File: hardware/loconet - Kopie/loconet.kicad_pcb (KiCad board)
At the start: 2 copper layers, 91.4 x 73.3 mm, 46 parts, among them J1 RJ12, J10 PWR, J11 PullUpEnable, J2 RJ12, J3 DCC, J4 Arduino Sockelleiste Pin01-15, J5 Arduino Sockelleiste Pin16-30, J6 PCA9685, J7 SCL/SDA, J8 I²C Connector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

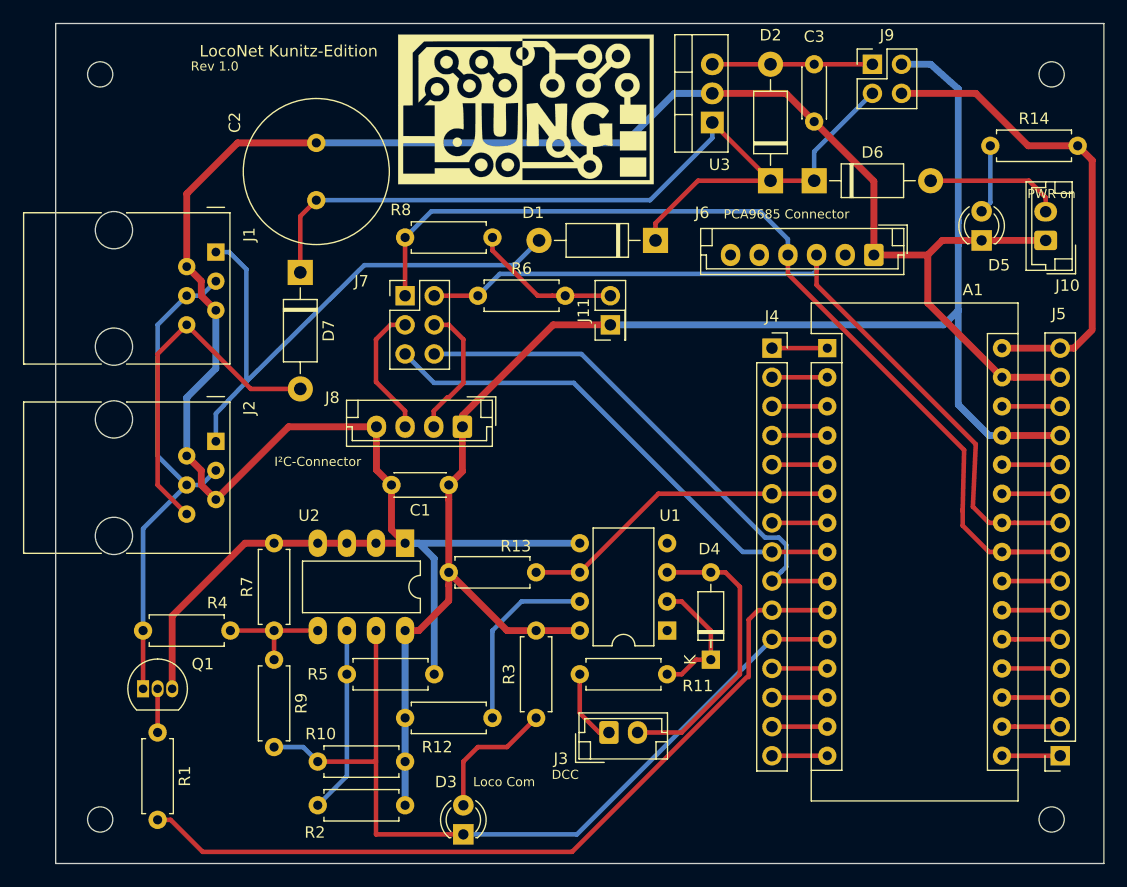
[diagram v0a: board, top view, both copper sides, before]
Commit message: Add variant hardware with loconet TX indicator LED
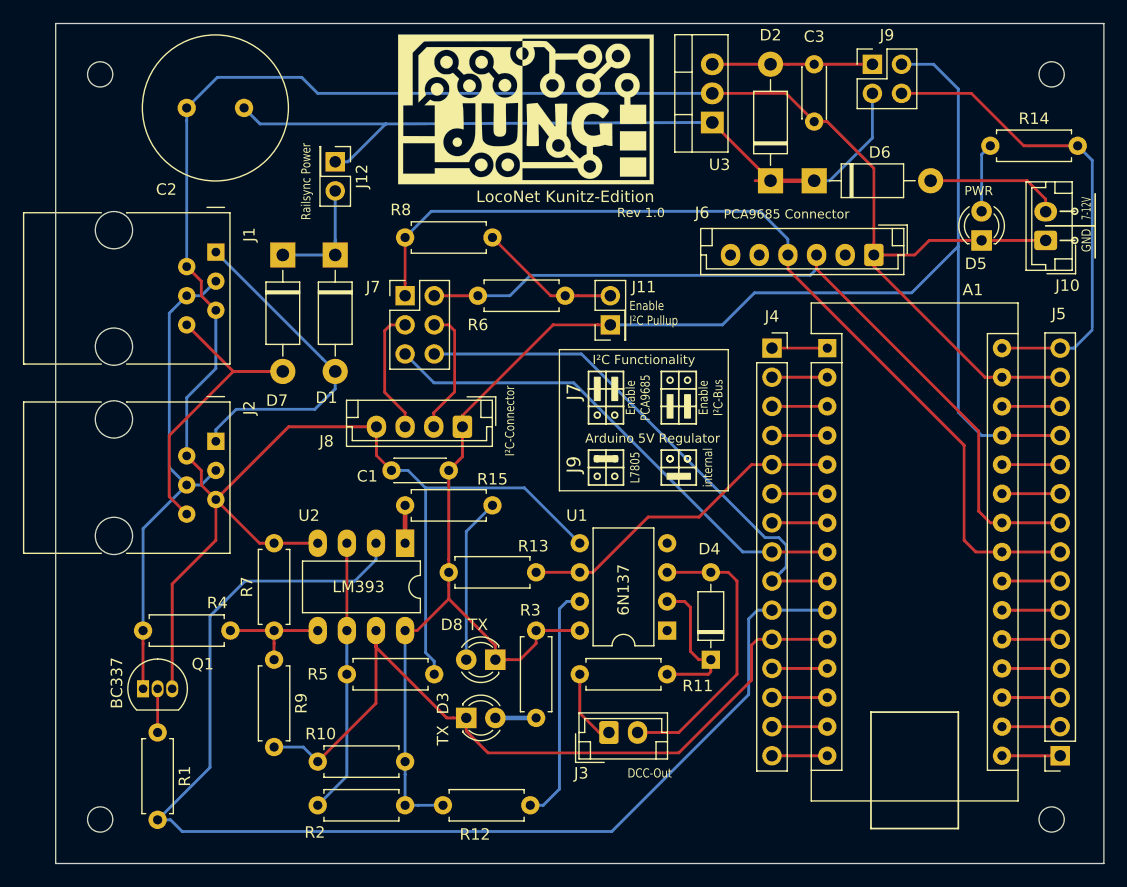
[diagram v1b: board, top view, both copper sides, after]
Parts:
- added D8: LocoTX, LED_THT:LED_D3.0mm, F.Cu at (236.5, 99.1)
- added J12: Railsync, Connector_PinHeader_2.54mm:PinHeader_2x01_P2.54mm_Vertical, F.Cu at (222.5, 55.6)
- added R15: 470k, Resistor_THT:R_Axial_DIN0207_L6.3mm_D2.5mm_P7.62mm_Horizontal, F.Cu at (236.2, 85.6)
- D3: value LocoCom -> LocoRX
- moved D1 28.0 mm to (222.5, 63.8), turned to 270 degrees
- moved C2 11.7 mm to (209.6, 50.9), turned to 0 degrees
- moved D3 10.2 mm to (233.9, 104.1), turned to 0 degrees
- moved R12 8.30 mm to (231.9, 111.8)
- moved D7 2.16 mm to (217.9, 63.8)
- moved C1 1.27 mm to (232.4, 82.5)
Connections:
- D1 pad 1: Vdrive -> Net-(D1-Pad1)
- D7 pad 1: Vdrive -> Net-(D1-Pad1)
- R2 pad 2: /Komperatorspannung -> U_Komperator
- R5 pad 1: /Komperatorspannung -> U_Komperator
- U2 pad 1: 29 -> Net-(R15-Pad2)
- U2 pad 2: 29 -> 10
- U2 pad 3: 29 -> U_Komperator
- U2 pad 6: /Komperatorspannung -> U_Komperator
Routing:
- net 10: track 71.1 -> 108.3 mm
- net U_Komperator: track 0.00 -> 23.9 mm
- net Net-(D1-Pad2): track 50.0 -> 29.2 mm
- net /Komperatorspannung: track 16.3 -> 0.00 mm
- net Net-(D8-Pad2): track 0.00 -> 14.4 mm
- net Net-(D1-Pad1): track 0.00 -> 11.5 mm
- net Vdrive: track 78.8 -> 70.1 mm
- net 29: track 222.5 -> 231.2 mm
- net Net-(D3-Pad2): track 11.7 -> 3.56 mm
- net 27: track 141.4 -> 149.3 mm
- net Net-(R12-Pad2): track 16.3 -> 20.9 mm
- net 11: track 73.6 -> 69.1 mm
- net Net-(R15-Pad2): track 0.00 -> 3.30 mm
- net Net-(D7-Pad2): track 30.8 -> 29.3 mm
- net Net-(D4-Pad1): track 11.7 -> 13.1 mm
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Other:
- board text added: "7-12V"
- board text added: "Arduino 5V Regulator"
- board text added: "DCC-Out"
- board text added: "Enable I²C Pullup"
- board text added: "Enable I²C-Bus"
- board text added: "Enable PCA9685"
- board text added: "GND"
- board text added: "I²C Functionality"
- board text added: "J7"
- board text added: "J9"
- board text added: "L7805"
- board text added: "PWR"
- board text added: "Railsync Power"
- board text added: "TX"
- board text added: "internal"
- board text removed: "DCC"
- board text removed: "Loco Com"
- board text removed: "PWR on"

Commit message: Einige Verbesserungen am PCB Layout
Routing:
- net Vdrive: track 70.1 -> 68.7 mm
- net 9: track 46.1 -> 46.9 mm
- net 11: track 69.1 -> 68.4 mm
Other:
- board text added: "1"
- board text added: "2"
- board text added: "3"
- board text added: "3V3"
- board text added: "4"
- board text added: "5"
- board text added: "5V"
- board text added: "6"
- board text added: "A0"
- board text added: "A1"
- board text added: "A2"
- board text added: "A3"
- board text added: "A4"
- board text added: "A5"
- board text added: "A6"
- board text added: "A7"
- board text added: "D10"
- board text added: "D11"
- board text added: "D12"
- board text added: "D13"
- board text added: "D2"
- board text added: "D3"
- board text added: "D4"
- board text added: "D5"
- board text added: "D6"
- board text added: "D7"
- board text added: "D8"
- board text added: "D9"
- board text added: "RST"
- board text added: "RX1"
- board text added: "TX1"
- board text added: "Vin"
- board text added: "Vref"

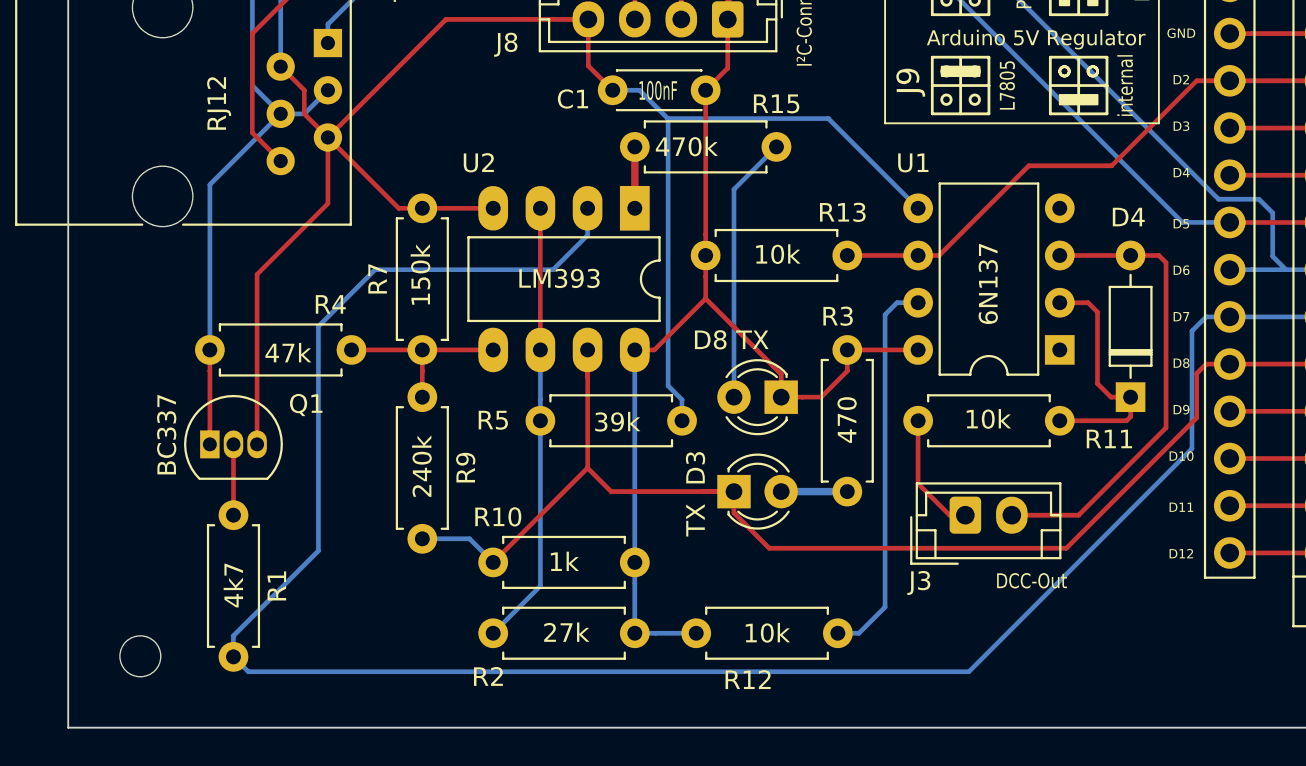
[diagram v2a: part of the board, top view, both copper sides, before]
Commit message: Added some capacitors
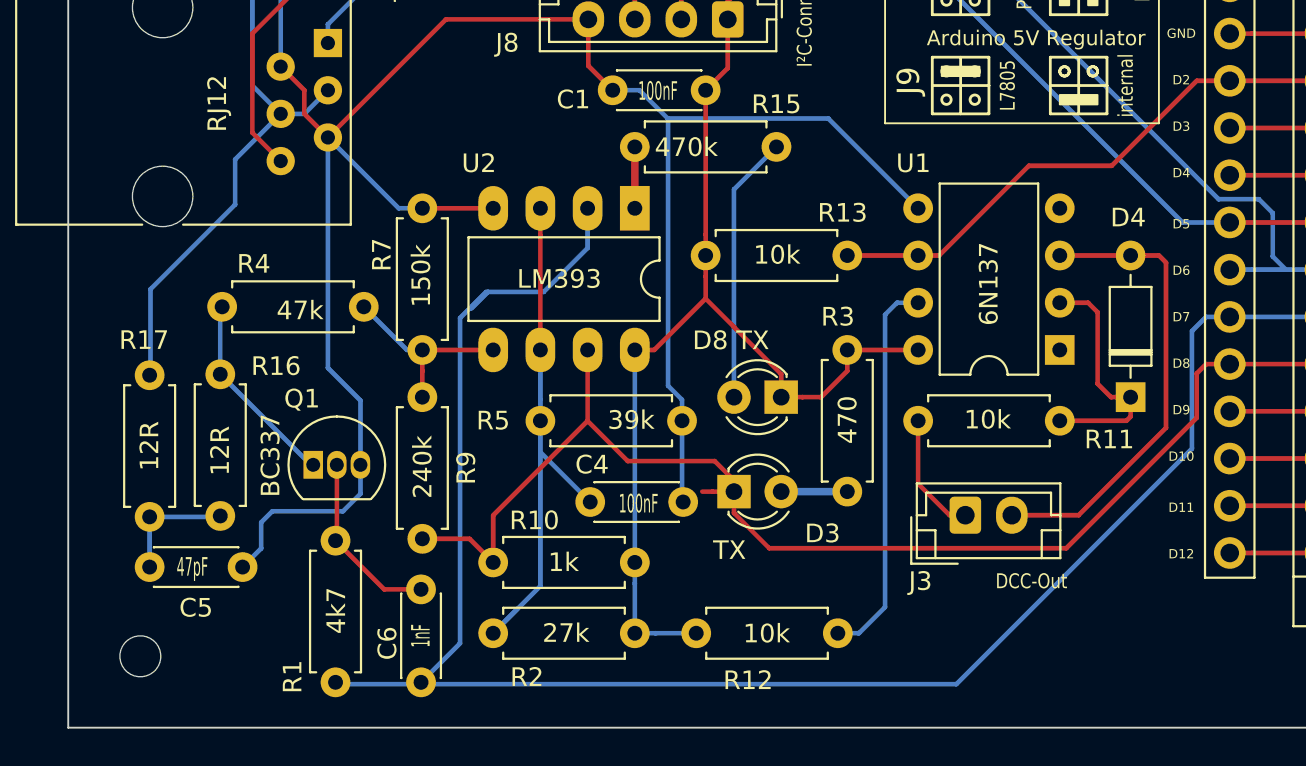
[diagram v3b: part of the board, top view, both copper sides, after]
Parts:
- added C4: 100nF, Capacitor_THT:C_Disc_D4.3mm_W1.9mm_P5.00mm, F.Cu at (226.2, 104.7)
- added C5: 47pF, Capacitor_THT:C_Disc_D4.3mm_W1.9mm_P5.00mm, F.Cu at (207.5, 108.2)
- added C6: 1nF, Capacitor_THT:C_Disc_D4.3mm_W1.9mm_P5.00mm, F.Cu at (217.1, 114.4)
- added R16: 12R, Resistor_THT:R_Axial_DIN0207_L6.3mm_D2.5mm_P7.62mm_Horizontal, F.Cu at (206.3, 105.5)
- added R17: 12R, Resistor_THT:R_Axial_DIN0207_L6.3mm_D2.5mm_P7.62mm_Horizontal, F.Cu at (202.5, 97.9)
- moved Q1 5.67 mm to (211.3, 102.7)
- moved R1 5.66 mm to (212.5, 106.8)
- moved R4 2.41 mm to (206.4, 94.2)
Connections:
- Q1 pad 1: LocoSignal -> Net-(Q1-Pad1)
- R4 pad 1: LocoSignal -> Net-(Q1-Pad1)
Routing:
- net 29: track 231.2 -> 246.2 mm
- net 10: track 108.0 -> 97.2 mm
- net Net-(Q1-Pad1): track 0.00 -> 10.7 mm
- net Net-(C5-Pad2): track 0.00 -> 6.52 mm
- net Net-(C6-Pad2): track 3.81 -> 9.79 mm
- net U_Komperator: track 23.9 -> 29.6 mm
- net LocoSignal: track 43.3 -> 40.9 mm
